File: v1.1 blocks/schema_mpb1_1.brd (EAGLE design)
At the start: 70.8 x 85.3 mm, 78 parts, among them IC1 CP2102, Q1 8M, Q2 32.768kHz, U1 NCP1117ST33T3G, U2 NCP1117ST50T3G, X2 PN61729-S, X5 POWERSUPPLY_DC21MMX

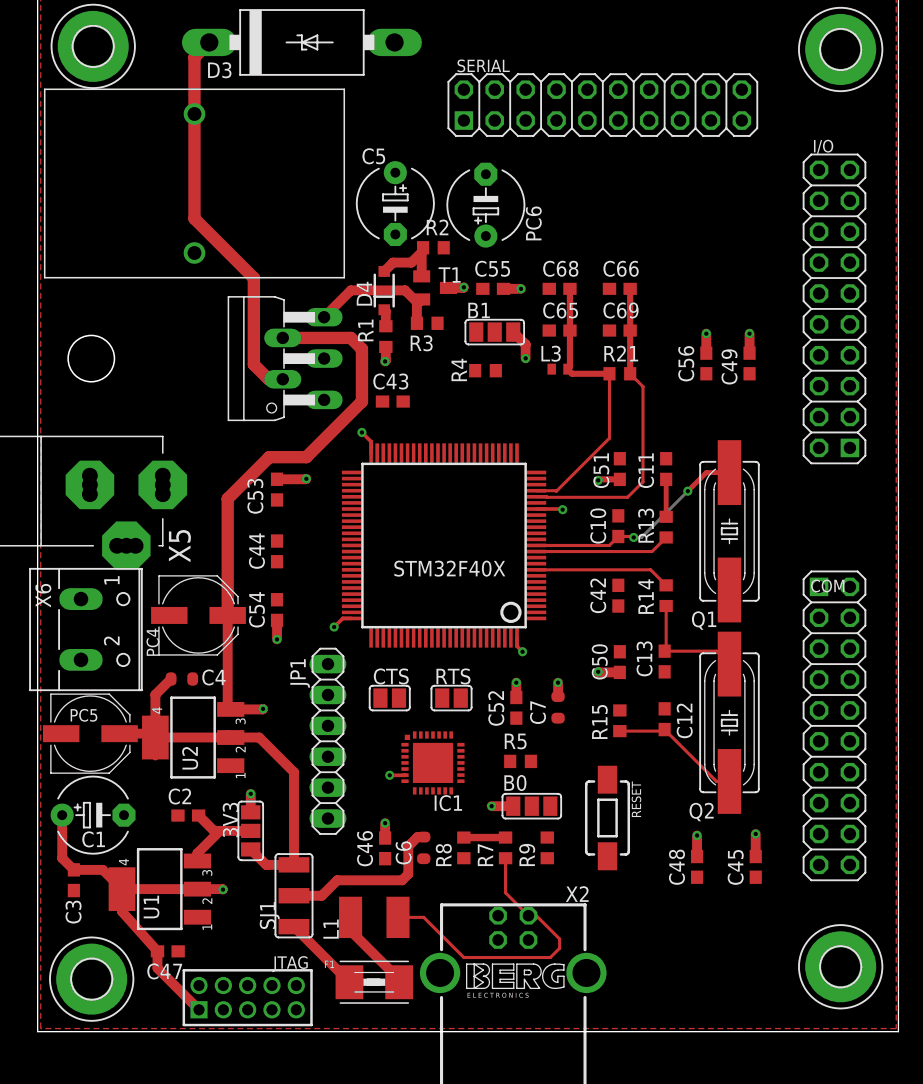
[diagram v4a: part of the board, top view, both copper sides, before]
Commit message: First Draft
Completed routing of first draft for main board
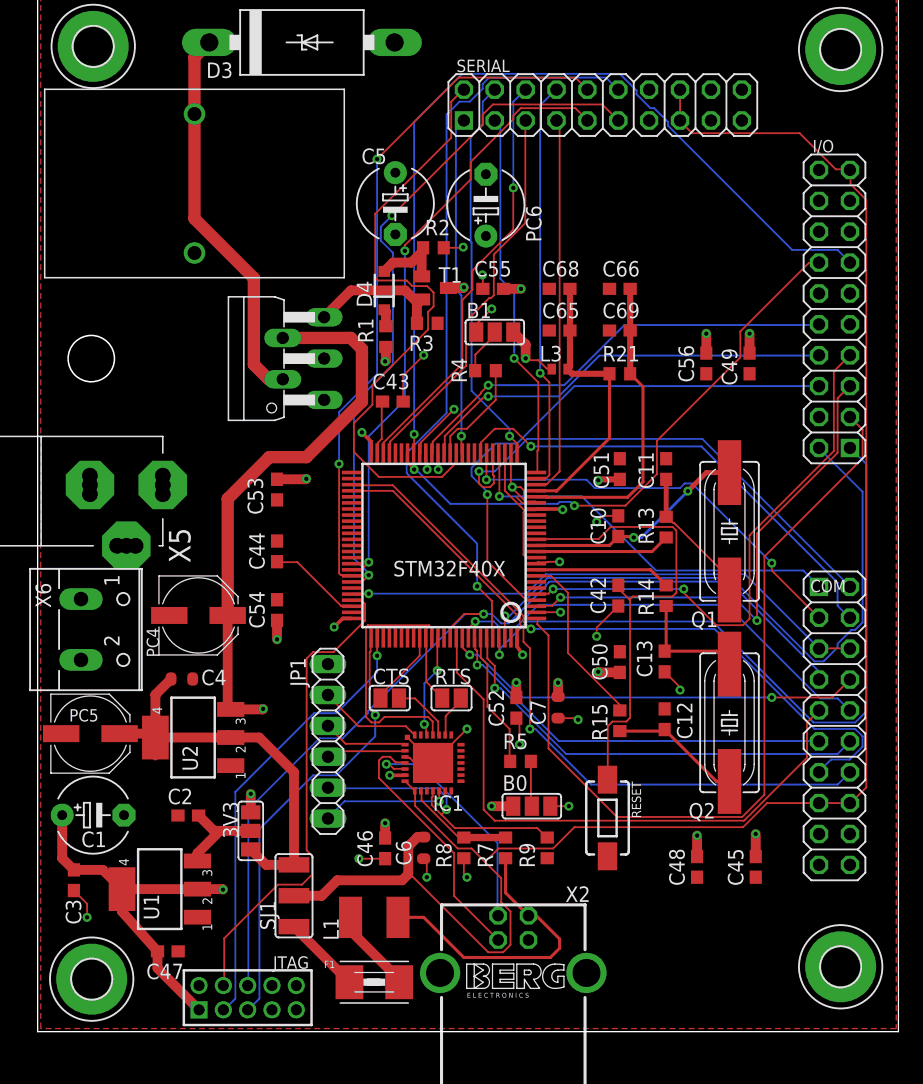
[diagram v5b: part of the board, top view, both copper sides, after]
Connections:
- removed net N$32: IC1.27, JP1.6
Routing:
- net +5V: track 14.0 -> 146.5 mm
- net NRF_SCK: track 0.00 -> 77.7 mm, vias 0 -> 1
- net PE12: track 0.00 -> 71.5 mm, vias 0 -> 1
- net PE2: track 0.00 -> 66.8 mm
- net RX6: track 0.00 -> 63.3 mm, vias 0 -> 1
- net PE0: track 0.00 -> 59.1 mm, vias 0 -> 1
- net TX6: track 0.00 -> 57.3 mm, vias 0 -> 2
- net RX5: track 0.00 -> 57.0 mm, vias 0 -> 2
- net USB_OTG_HS_DP: track 0.00 -> 56.3 mm, vias 0 -> 1
- net USB_OTG_HS_DM: track 0.00 -> 56.2 mm, vias 0 -> 1
- net PE1: track 0.00 -> 52.7 mm, vias 0 -> 1
- net GND: track 0.00 -> 51.9 mm, vias 0 -> 17
- net RX1: track 0.00 -> 50.2 mm
- net TX5: track 0.00 -> 50.1 mm, vias 0 -> 2
- net NRF_MISO: track 0.00 -> 48.5 mm
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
